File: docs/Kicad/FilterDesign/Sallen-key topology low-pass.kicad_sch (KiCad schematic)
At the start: 6 parts, among them J3 Conn_01x02_Pin, J4 ${SIM.PARAMS}, U1 LM324

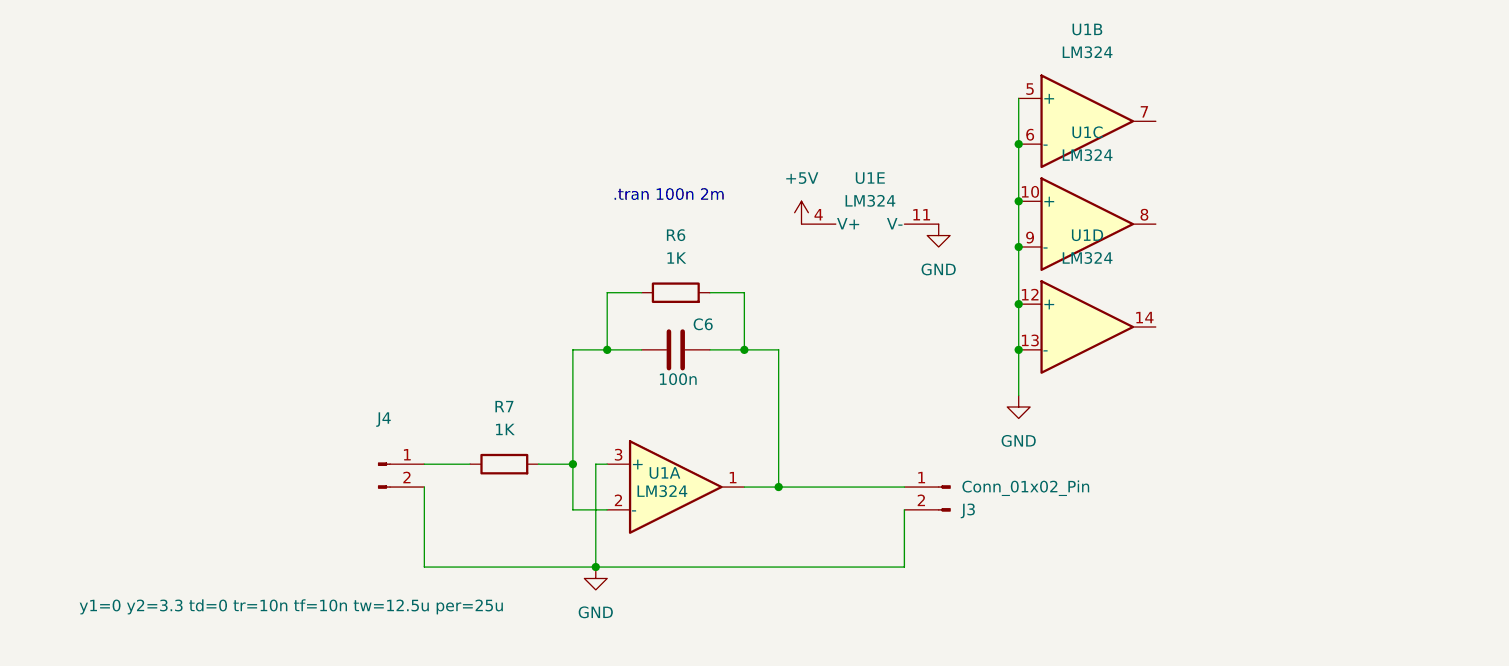
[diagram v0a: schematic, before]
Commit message: Sallen-key topology low-pass filter tilføjet i kicad
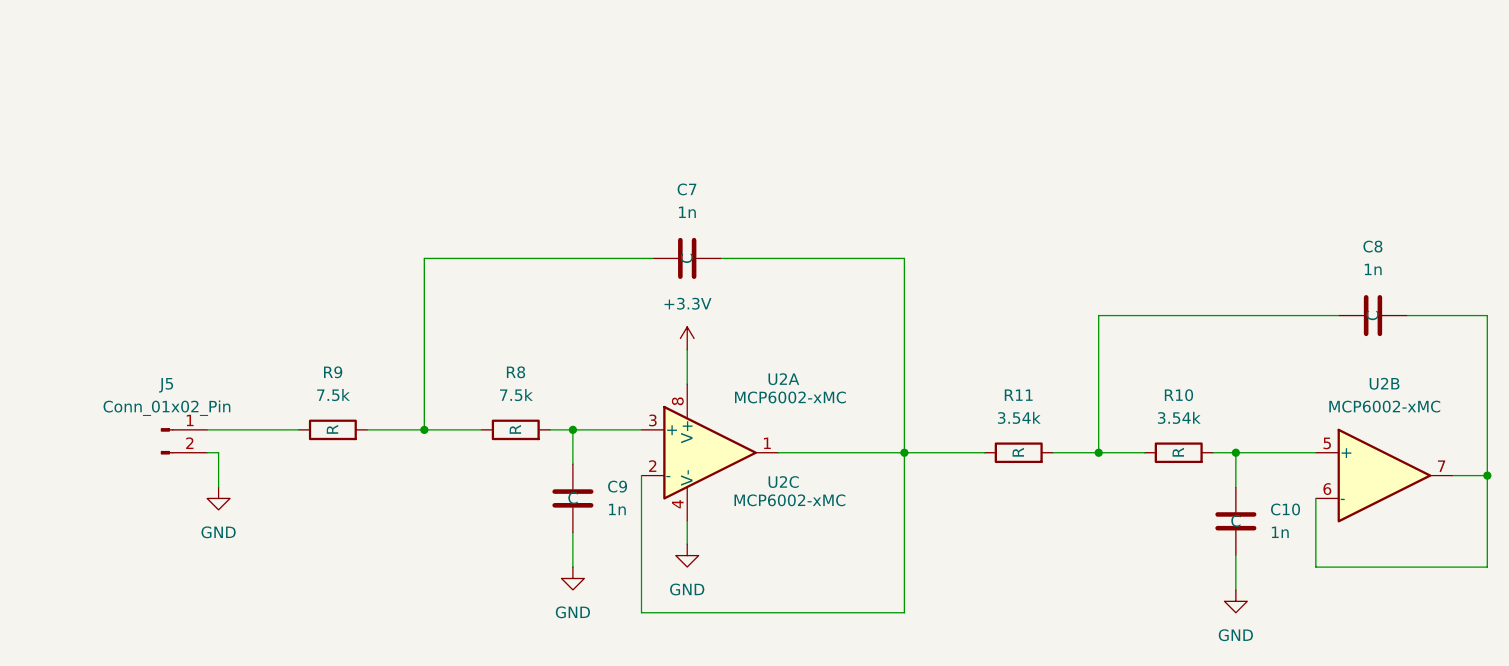
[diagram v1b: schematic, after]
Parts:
- removed C6: 100n, symbol Device:C
- removed J3: Conn_01x02_Pin, symbol Connector:Conn_01x02_Pin
- removed J4: ${SIM.PARAMS}, symbol Connector:Conn_01x02_Pin
- removed R6, R7: 1K, symbol Device:R
- removed U1: LM324, symbol Amplifier_Operational:LM324
- added C10, C7, C8, C9: 1n, symbol Device:C
- added J5: Conn_01x02_Pin, symbol Connector:Conn_01x02_Pin
- added R10, R11: 3.54k, symbol Device:R
- added R8, R9: 7.5k, symbol Device:R
- added U2: MCP6002-xMC, Package_DFN_QFN:DFN-8-1EP_3x2mm_P0.5mm_EP1.75x1.45mm, symbol Amplifier_Operational:MCP6002-xMC
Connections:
- net GND: now also C10.2, C9.2, J5.2 (Pin_2), U2.4 (V-), U2.9 (V-)
- new net: C10.1, R10.2, U2.5 (+)
- new net: C7.2, R11.1, U2.1, U2.2 (-)
- new net: C9.1, R8.2, U2.3 (+)
- new net: C7.1, R8.1, R9.2
- new net: C8.1, R10.1, R11.2
- new net: C8.2, U2.6 (-), U2.7
- new net: J5.1 (Pin_1), R9.1
- new net +3.3V: U2.8 (V+)
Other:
- note removed: ".tran 100n 2m"
